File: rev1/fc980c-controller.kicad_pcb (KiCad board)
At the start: 2 copper layers, 82.2 x 35.5 mm, 36 parts, among them J1 SWD, J2 USB, J3 KEYBOARD, SW1 BOOT0, U1 XC6206P332MR, U2 STM32F401CBUx, U3 USBLC6-2SC6, U4 M24C64-RMN6TP, U5 PCA9306DC, Y1 8MHz Cl 20pF

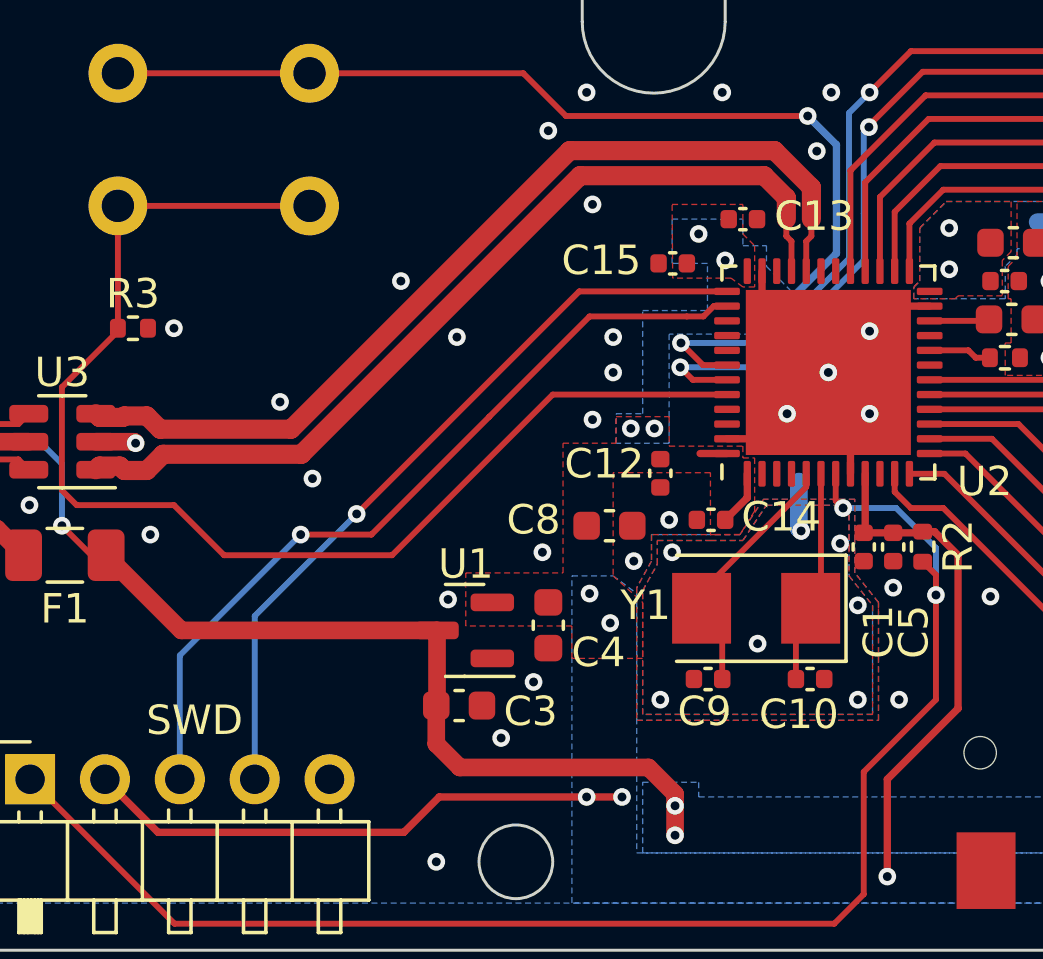
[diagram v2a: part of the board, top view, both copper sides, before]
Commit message: rev2: Fix SWDIO MCU pin
Didn't take long to find flaws in the revision 1 design. SWDIO is
erroneously hooked up to PA15 on the MCU instead of PA13.
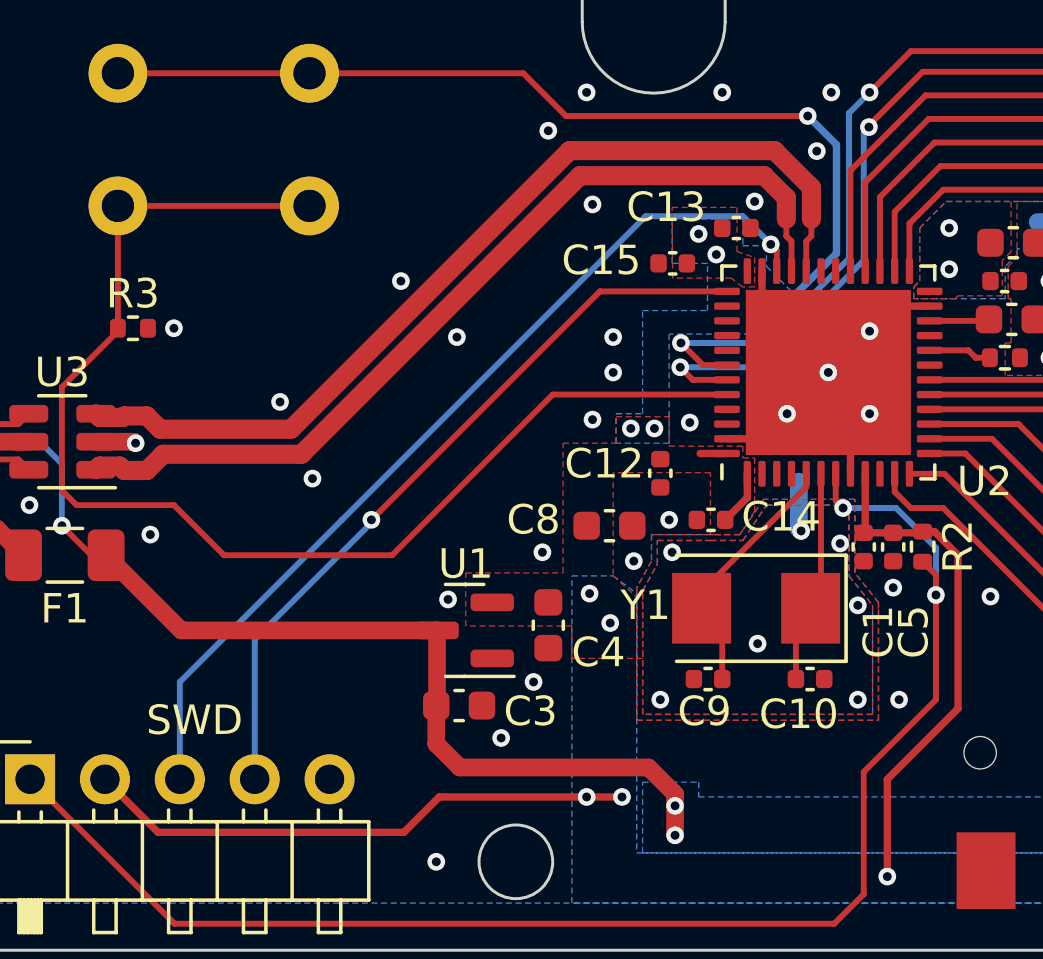
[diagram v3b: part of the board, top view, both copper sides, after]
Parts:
- moved C13 0.37 mm to (114.0, 46.5)
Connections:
- U2 pad 34: unconnected-(U2-Pad34) -> SWDIO
- U2 pad 38: SWDIO -> unconnected-(U2-Pad38)
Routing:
- net SWDIO: track 27.7 -> 31.3 mm
- net GND: vias 60 -> 62
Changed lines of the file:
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@@
   (net 36 "unconnected-(U2-Pad40)")
   (net 37 "unconnected-(U2-Pad31)")
-  (net 38 "unconnected-(U2-Pad34)")
+  (net 38 "unconnected-(U2-Pad38)")
   (net 39 "unconnected-(U2-Pad45)")
   (net 40 "unconnected-(U2-Pad41)")
@@
     (property "Sheetfile" "fc980c-controller.kicad_sch")
     (property "Sheetname" "")
-    (attr exclude_from_pos_files exclude_from_bom)
+    (attr exclude_from_pos_files)
     (fp_text reference "LOGO1" (at 0 0) (layer "F.SilkS") hide
       (effects (font (size 1 1) (thickness 0.15)))
@@
     (property "Sheetfile" "fc980c-controller.kicad_sch")
     (property "Sheetname" "")
-    (attr exclude_from_pos_files exclude_from_bom)
+    (attr exclude_from_pos_files)
     (fp_text reference "H2" (at 0 -3.2) (layer "F.SilkS") hide
       (effects (font (size 1 1) (thickness 0.15)))
@@
     (property "Sheetfile" "fc980c-controller.kicad_sch")
     (property "Sheetname" "")
-    (attr exclude_from_pos_files exclude_from_bom)
+    (attr exclude_from_pos_files)
     (fp_text reference "H1" (at 0 -3.2) (layer "F.SilkS") hide
       (effects (font (size 1 1) (thickness 0.15)))
@@
   )
   (footprint "Capacitor_SMD:C_0402_1005Metric" (layer "F.Cu")
-    (at 114.2 46.2)
+    (at 113.98 46.5)
     (descr "Capacitor SMD 0402 (1005 Metric), square (rectangular) end terminal, IPC_7351 nominal, (Body size source: IPC-SM-782 page 76, https://www.pcb-3d.com/wordpress/wp-content/uploads/ipc-sm-782a_amendment_1_and_2.pdf), generated with kicad-footprint-generator")
     (tags "capacitor")
@@
     (property "Sheetname" "")
     (attr smd)
-    (fp_text reference "C13" (at 2.42 -0.1) (layer "F.SilkS")
+    (fp_text reference "C13" (at -2.38 -0.7) (layer "F.SilkS")
       (effects (font (size 1 1) (thickness 0.15)))
     )
@@
       (net 27 "D_P") (pinfunction "PA12") (pintype "bidirectional"))
     (pad "34" smd roundrect (at 3.4375 -1.75 90) (size 0.875 0.25) (layers "F.Cu" "F.Paste" "F.Mask") (roundrect_rratio 0.25)
-      (net 38 "unconnected-(U2-Pad34)") (pinfunction "PA13") (pintype "bidirectional+no_connect"))
+      (net 7 "SWDIO") (pinfunction "PA13") (pintype "bidirectional"))
     (pad "35" smd roundrect (at 3.4375 -2.25 90) (size 0.875 0.25) (layers "F.Cu" "F.Paste" "F.Mask") (roundrect_rratio 0.25)
       (net 1 "GND") (pinfunction "VSS") (pintype "power_in"))
@@
       (net 8 "SWCLK") (pinfunction "PA14") (pintype "bidirectional"))
     (pad "38" smd roundrect (at 2.25 -3.4375 90) (size 0.25 0.875) (layers "F.Cu" "F.Paste" "F.Mask") (roundrect_rratio 0.25)
-      (net 7 "SWDIO") (pinfunction "PA15") (pintype "bidirectional"))
+      (net 38 "unconnected-(U2-Pad38)") (pinfunction "PA15") (pintype "bidirectional+no_connect"))
     (pad "39" smd roundrect (at 1.75 -3.4375 90) (size 0.25 0.875) (layers "F.Cu" "F.Paste" "F.Mask") (roundrect_rratio 0.25)
       (net 35 "unconnected-(U2-Pad39)") (pinfunction "PB3") (pintype "bidirectional+no_connect"))
@@
   (via (at 107.1 61.9) (size 0.6) (drill 0.3) (layers "F.Cu" "B.Cu") (free) (net 1))
   (via (at 141 52.9) (size 0.6) (drill 0.3) (layers "F.Cu" "B.Cu") (net 1))
+  (via (at 114.6 45.6) (size 0.6) (drill 0.3) (layers "F.Cu" "B.Cu") (free) (net 1))
   (via (at 155.8 69.9) (size 0.6) (drill 0.3) (layers "F.Cu" "B.Cu") (free) (net 1))
   (via (at 147.3 61.5) (size 0.6) (drill 0.3) (layers "F.Cu" "B.Cu") (net 1))
@@
   (via (at 116.708411 43.891589) (size 0.6) (drill 0.3) (layers "F.Cu" "B.Cu") (free) (net 1))
   (via (at 94.9 49.9) (size 0.6) (drill 0.3) (layers "F.Cu" "B.Cu") (free) (net 1))
+  (via (at 112.4 53.1) (size 0.6) (drill 0.3) (layers "F.Cu" "B.Cu") (free) (net 1))
   (via (at 117.5 57.2) (size 0.6) (drill 0.3) (layers "F.Cu" "B.Cu") (free) (net 1))
   (via (at 103.8 68) (size 0.6) (drill 0.3) (layers "F.Cu" "B.Cu") (free) (net 1))
@@
   (segment (start 120.7 56.8) (end 121.5 57.6) (width 0.25) (layer "F.Cu") (net 2))
   (via (at 119.1 68.5) (size 0.6) (drill 0.3) (layers "F.Cu" "B.Cu") (free) (net 2))
-  (via (at 113.6 47.6) (size 0.6) (drill 0.3) (layers "F.Cu" "B.Cu") (free) (net 2))
+  (via (at 113.3 47.4) (size 0.6) (drill 0.3) (layers "F.Cu" "B.Cu") (free) (net 2))
   (via (at 144.85 68.85) (size 0.6) (drill 0.3) (layers "F.Cu" "B.Cu") (free) (net 2))
   (via (at 110.4 53.3) (size 0.6) (drill 0.3) (layers "F.Cu" "B.Cu") (free) (net 2))
@@
   (segment (start 119.4 56) (end 117.6 56) (width 0.2) (layer "B.Cu") (net 6))
   (segment (start 120.75 57.35) (end 119.4 56) (width 0.2) (layer "B.Cu") (net 6))
-  (segment (start 112.862348 49.5) (end 112.3 49.5) (width 0.2) (layer "F.Cu") (net 7))
-  (segment (start 101.6 56.9) (end 99.2 56.9) (width 0.2) (layer "F.Cu") (net 7))
-  (segment (start 113.6625 49.15) (end 113.212348 49.15) (width 0.2) (layer "F.Cu") (net 7))
-  (segment (start 105.6 52.9) (end 101.6 56.9) (width 0.2) (layer "F.Cu") (net 7))
-  (segment (start 113.212348 49.15) (end 112.862348 49.5) (width 0.2) (layer "F.Cu") (net 7))
-  (segment (start 112.3 49.5) (end 109 49.5) (width 0.2) (layer "F.Cu") (net 7))
-  (segment (start 109 49.5) (end 105.6 52.9) (width 0.2) (layer "F.Cu") (net 7))
-  (via (at 99.2 56.9) (size 0.6) (drill 0.3) (layers "F.Cu" "B.Cu") (net 7))
-  (segment (start 95.1 61) (end 95.1 65.2) (width 0.2) (layer "B.Cu") (net 7))
-  (segment (start 99.2 56.9) (end 95.1 61) (width 0.2) (layer "B.Cu") (net 7))
-  (segment (start 113.6625 48.65) (end 108.65 48.65) (width 0.2) (layer "F.Cu") (net 8))
-  (segment (start 108.65 48.65) (end 101.1 56.2) (width 0.2) (layer "F.Cu") (net 8))
-  (via (at 101.1 56.2) (size 0.6) (drill 0.3) (layers "F.Cu" "B.Cu") (net 8))
-  (segment (start 101.1 56.2) (end 97.64 59.66) (width 0.2) (layer "B.Cu") (net 8))
-  (segment (start 97.64 59.66) (end 97.64 65.2) (width 0.2) (layer "B.Cu") (net 8))
+  (segment (start 115.35 47.9625) (end 115.35 47.260452) (width 0.2) (layer "F.Cu") (net 7))
+  (segment (start 115.35 47.260452) (end 115.145305 47.055757) (width 0.2) (layer "F.Cu") (net 7))
+  (via (at 115.145305 47.055757) (size 0.6) (drill 0.3) (layers "F.Cu" "B.Cu") (net 7))
+  (segment (start 100.6 56.4) (end 110.9 46.1) (width 0.2) (layer "B.Cu") (net 7))
+  (segment (start 95.1 61.9) (end 95.1 65.2) (width 0.2) (layer "B.Cu") (net 7))
+  (segment (start 114.2 46.1) (end 115.145305 47.045305) (width 0.2) (layer "B.Cu") (net 7))
+  (segment (start 100.6 56.4) (end 95.1 61.9) (width 0.2) (layer "B.Cu") (net 7))
+  (segment (start 110.9 46.1) (end 114.2 46.1) (width 0.2) (layer "B.Cu") (net 7))
+  (segment (start 115.145305 47.045305) (end 115.145305 47.055757) (width 0.2) (layer "B.Cu") (net 7))
+  (segment (start 101.6 56.4) (end 109.35 48.65) (width 0.2) (layer "F.Cu") (net 8))
+  (segment (start 109.35 48.65) (end 113.6625 48.65) (width 0.2) (layer "F.Cu") (net 8))
+  (via (at 101.6 56.4) (size 0.6) (drill 0.3) (layers "F.Cu" "B.Cu") (net 8))
+  (segment (start 97.64 60.46) (end 97.64 65.2) (width 0.2) (layer "B.Cu") (net 8))
+  (segment (start 101.6 56.4) (end 101.6 56.5) (width 0.2) (layer "B.Cu") (net 8))
+  (segment (start 101.6 56.5) (end 97.64 60.46) (width 0.2) (layer "B.Cu") (net 8))
   (segment (start 87.8 53.975001) (end 84.7 53.975) (width 0.2) (layer "F.Cu") (net 9))
   (segment (start 89.975 54.7) (end 89.625 54.35) (width 0.2) (layer "F.Cu") (net 9))
@@
   (segment (start 141.4 54.8) (end 140.9 54.8) (width 0.2) (layer "F.Cu") (net 48))
   (segment (start 139.9 55.3) (end 140.4 55.3) (width 0.2) (layer "F.Cu") (net 48))
-  (zone (net 0) (net_name "") (layer "F.Cu") (hatch edge 0.508)
-    (connect_pads (clearance 0))
-    (min_thickness 0.15)
-    (keepout (tracks allowed) (vias allowed) (pads allowed) (copperpour not_allowed) (footprints allowed))
-    (fill (thermal_gap 0.2) (thermal_bridge_width 0.508))
-    (polygon
-      (pts
-        (xy 107.7 52)
-        (xy 107.3 52.4)
-        (xy 106.8 51.8)
-        (xy 107.218032 51.401641)
-      )
-    )
-  )
   (zone (net 2) (net_name "VDDA") (layer "F.Cu") (hatch edge 0.508)
     (priority 1)
@@
     (polygon
       (pts
-        (xy 114.2 46.7)
-        (xy 114.6 47.1)
+        (xy 114 47.3)
+        (xy 114.6 47.5)
         (xy 114.6 48.5)
         (xy 114.2 48.5)
         (xy 113.8 48.2)
         (xy 111.82 48.2)
-        (xy 111.8 45.7)
-        (xy 114.2 45.7)
+        (xy 111.8 45.8)
+        (xy 114 45.8)
       )
     )
@@
   (zone (net 0) (net_name "") (layer "F.Cu") (hatch edge 0.508)
     (connect_pads (clearance 0))
+    (min_thickness 0.254)
+    (keepout (tracks allowed) (vias allowed) (pads allowed) (copperpour not_allowed) (footprints allowed))
+    (fill (thermal_gap 0.508) (thermal_bridge_width 0.508))
+    (polygon
+      (pts
+        (xy 114.7 47.2)
+        (xy 114.1 47.2)
+        (xy 114.1 46.9)
+        (xy 114.7 46.9)
+      )
+    )
+  )
+  (zone (net 0) (net_name "") (layer "F.Cu") (hatch edge 0.508)
+    (connect_pads (clearance 0))
     (min_thickness 0.15)
     (keepout (tracks allowed) (vias allowed) (pads allowed) (copperpour not_allowed) (footprints allowed))
@@
     )
   )
+  (zone (net 0) (net_name "") (layer "B.Cu") (hatch edge 0.508)
+    (connect_pads (clearance 0))
+    (min_thickness 0.254)
+    (keepout (tracks allowed) (vias allowed) (pads allowed) (copperpour not_allowed) (footprints allowed))
+    (fill (thermal_gap 0.508) (thermal_bridge_width 0.508))
+    (polygon
+      (pts
+        (xy 97.6 60.5)
+        (xy 96.7 60.5)
+        (xy 96.7 60.3)
+        (xy 97.6 60.3)
+      )
+    )
+  )
   (zone (net 1) (net_name "GND") (layer "B.Cu") (hatch edge 0.508)
     (connect_pads (clearance 0.15))
@@
       )
     )
-  )
-  (zone (net 0) (net_name "") (layer "B.Cu") (hatch edge 0.508)
-    (connect_pads (clearance 0))
-    (min_thickness 0.15)
-    (keepout (tracks allowed) (vias allowed) (pads allowed) (copperpour not_allowed) (footprints allowed))
-    (fill (thermal_gap 0.2) (thermal_bridge_width 0.508))
-    (polygon
-      (pts
-        (xy 97.6 59.6)
-        (xy 96.7 59.6)
-        (xy 96.7 59.3)
-        (xy 97.6 59.3)
-      )
-    )

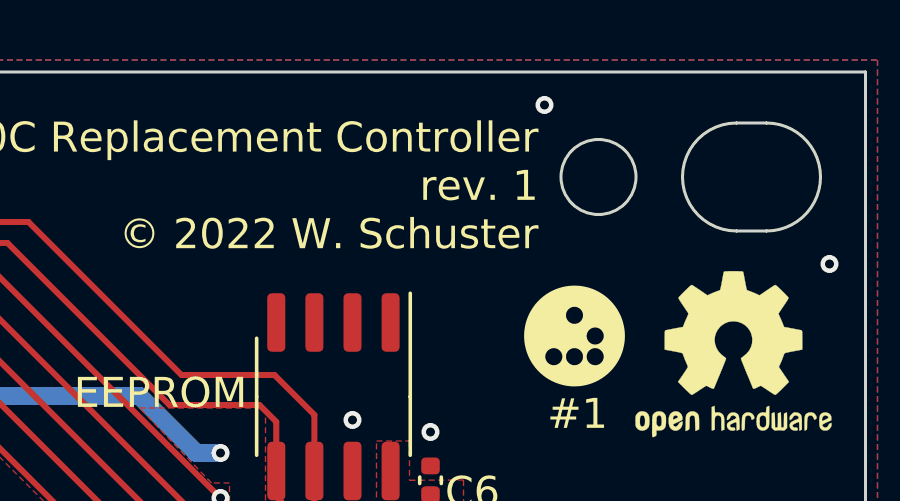
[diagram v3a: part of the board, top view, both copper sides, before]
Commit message: rev2: Update revision references in schematic and PCB
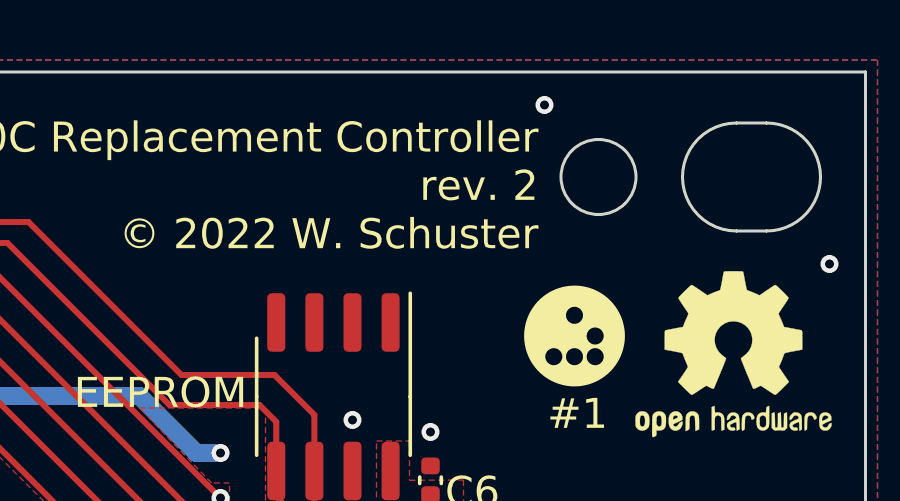
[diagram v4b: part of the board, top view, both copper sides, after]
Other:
- board text added: "Leopold FC980C Replacement Controller rev. 2 © 2022 W. Schuster"
- board text removed: "Leopold FC980C Replacement Controller rev. 1 © 2022 W. Schuster"
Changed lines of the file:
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@@
   (title_block
     (title "Leopold FC980C Replacement Controller")
-    (rev "1")
+    (rev "2")
     (company "Wilhelm Schuster")
     (comment 1 "Licensed under CERN-OHL-S V2")
@@
     (effects (font (size 1 1) (thickness 0.15)))
   )
-  (gr_text "Leopold FC980C Replacement Controller\nrev. 1\n© 2022 W. Schuster" (at 146.1 39.3) (layer "F.SilkS")
+  (gr_text "Leopold FC980C Replacement Controller\nrev. 2\n© 2022 W. Schuster" (at 146.1 39.3) (layer "F.SilkS")
     (effects (font (size 1 1) (thickness 0.15)) (justify right))
   )
